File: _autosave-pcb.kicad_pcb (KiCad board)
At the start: 2 copper layers, 65 x 56 mm, 50 parts, among them J1 Raspberry_Pi_2_3, J10 Conn_01x03_Male, J11 Conn_01x03_Male, J12 Conn_01x03_Male, J13 Conn_01x03_Male, J14 Conn_01x02_Male, J16 Conn_01x02_Male, J17 Conn_01x02_Male, J2 Conn_01x03_Male, J3 Conn_01x03_Male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

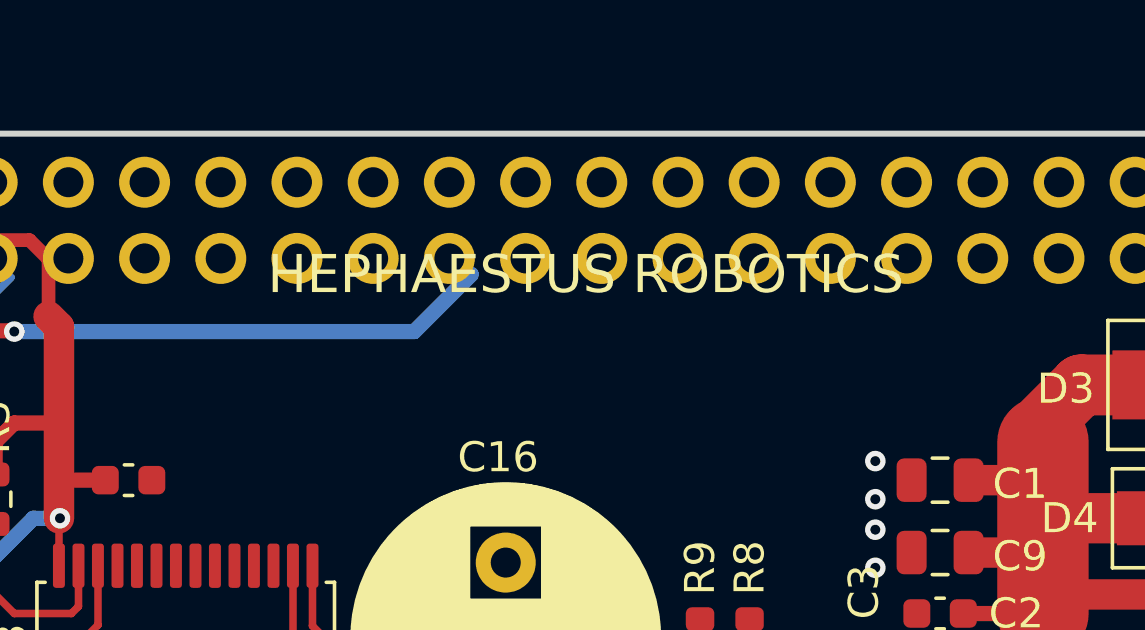
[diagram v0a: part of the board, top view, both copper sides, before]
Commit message: Added slit for ribbon cable from pi camera
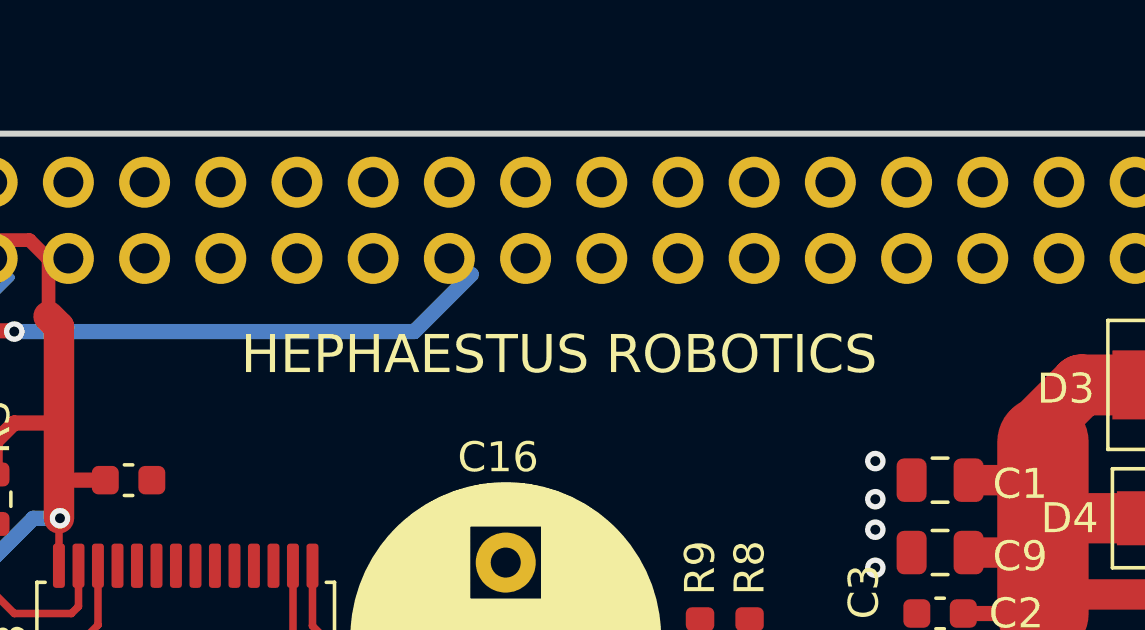
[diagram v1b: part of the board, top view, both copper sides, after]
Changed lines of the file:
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@@
     (effects (font (size 1 1) (thickness 0.25)))
   )
-  (gr_text "HEPHAESTUS ROBOTICS" (at 125.73 75.692) (layer "F.SilkS")
+  (gr_text "HEPHAESTUS ROBOTICS" (at 124.841 78.359) (layer "F.SilkS")
     (effects (font (size 1.27 1.27) (thickness 0.15)))
   )
